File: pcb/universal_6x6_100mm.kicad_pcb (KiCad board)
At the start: 2 copper layers, 100 x 100 mm, 88 parts

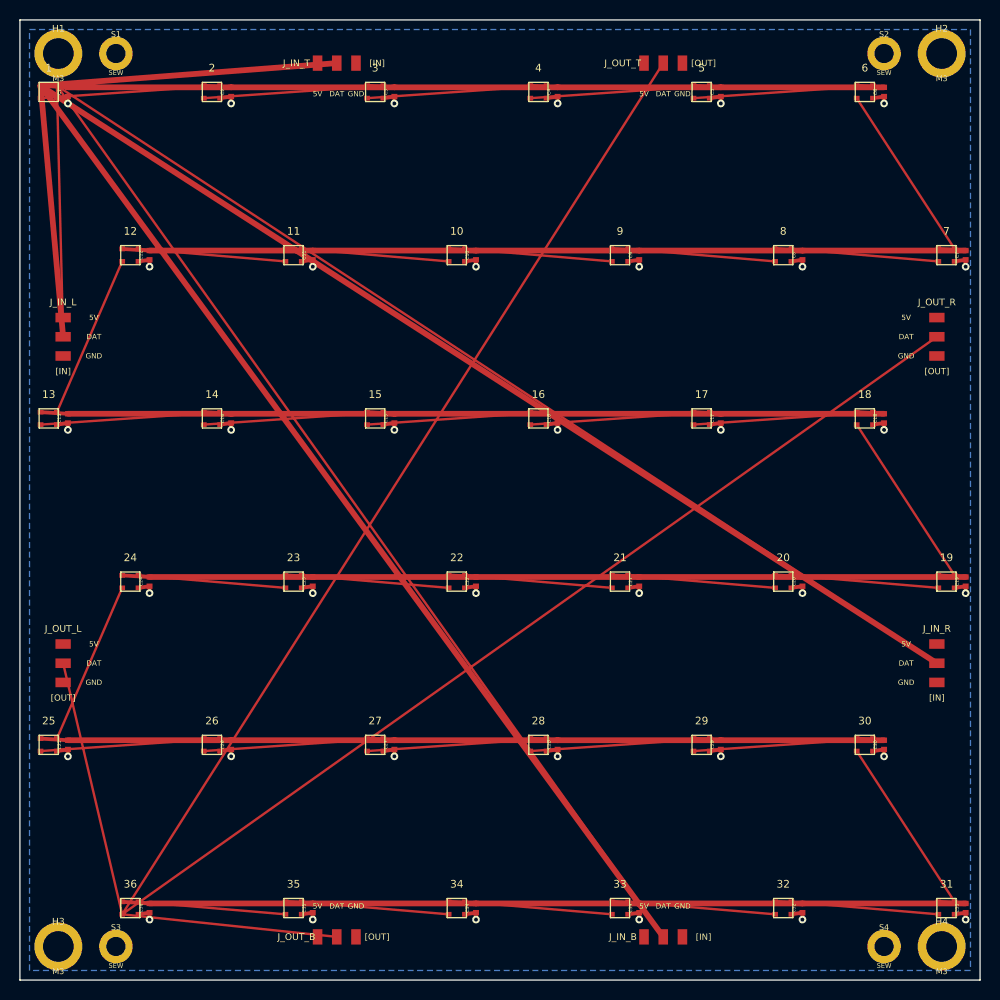
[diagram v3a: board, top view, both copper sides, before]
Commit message: feat: set back 8-port JST matrix 10mm into valleys for diagonal 50mm cable fit and zero overlap
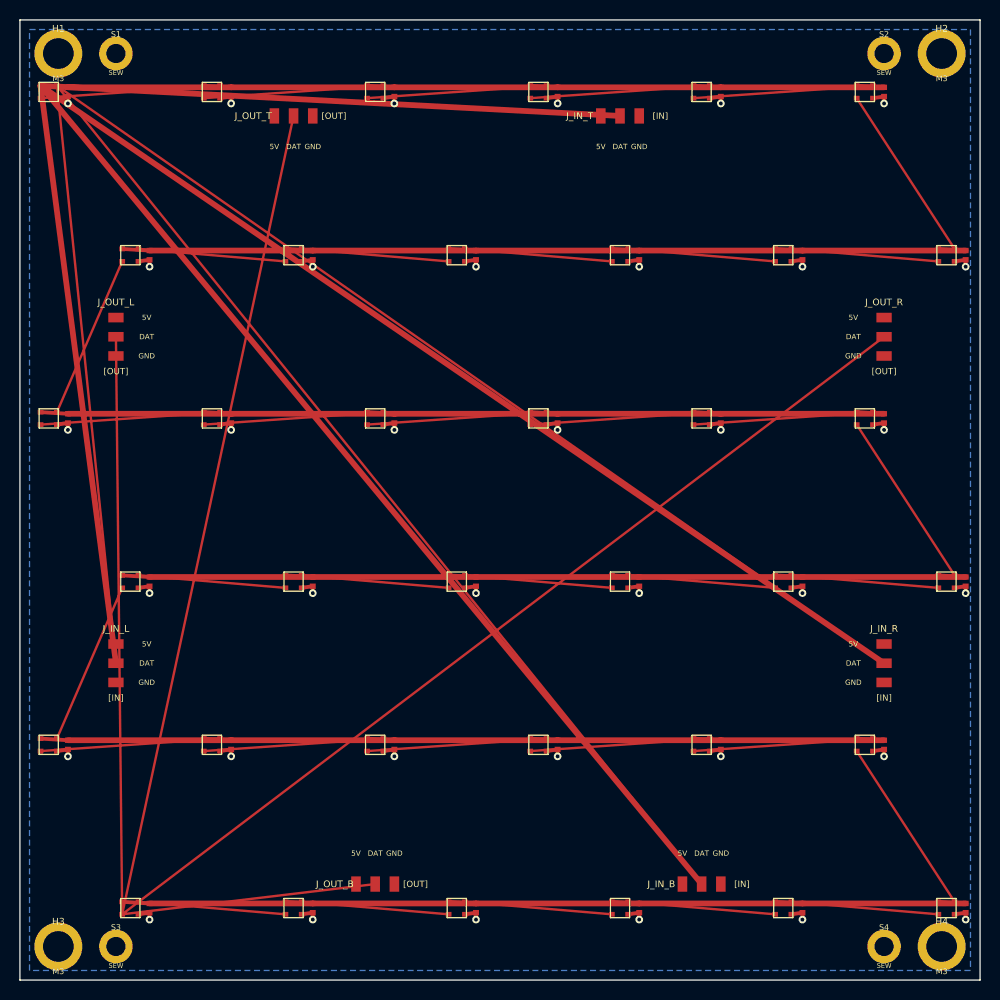
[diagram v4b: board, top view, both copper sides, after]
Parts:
- removed 1, 10, 11, 12, 13, 14, 15, 16, 17, 18, 19, 2, 20, 21, 22, 23, 24, 25, 26, 27, 28, 29, 3, 30, 31, 32, 33, 34, 35, 36, 4, 5, 6, 7, 8, 9: , LED_SMD:LED_WS2812B_PLCC4_2.0x2.0mm
- added D1: , LED_SMD:LED_WS2812B_PLCC4_2.0x2.0mm, F.Cu at (3.00, 7.50)
- added D10: , LED_SMD:LED_WS2812B_PLCC4_2.0x2.0mm, F.Cu at (45.5, 24.5)
- added D11: , LED_SMD:LED_WS2812B_PLCC4_2.0x2.0mm, F.Cu at (28.5, 24.5)
- added D12: , LED_SMD:LED_WS2812B_PLCC4_2.0x2.0mm, F.Cu at (11.5, 24.5)
- added D13: , LED_SMD:LED_WS2812B_PLCC4_2.0x2.0mm, F.Cu at (3.00, 41.5)
- added D14: , LED_SMD:LED_WS2812B_PLCC4_2.0x2.0mm, F.Cu at (20.0, 41.5)
- added D15: , LED_SMD:LED_WS2812B_PLCC4_2.0x2.0mm, F.Cu at (37.0, 41.5)
- added D16: , LED_SMD:LED_WS2812B_PLCC4_2.0x2.0mm, F.Cu at (54.0, 41.5)
- added D17: , LED_SMD:LED_WS2812B_PLCC4_2.0x2.0mm, F.Cu at (71.0, 41.5)
- added D18: , LED_SMD:LED_WS2812B_PLCC4_2.0x2.0mm, F.Cu at (88.0, 41.5)
- added D19: , LED_SMD:LED_WS2812B_PLCC4_2.0x2.0mm, F.Cu at (96.5, 58.5)
- added D2: , LED_SMD:LED_WS2812B_PLCC4_2.0x2.0mm, F.Cu at (20.0, 7.50)
- added D20: , LED_SMD:LED_WS2812B_PLCC4_2.0x2.0mm, F.Cu at (79.5, 58.5)
- added D21: , LED_SMD:LED_WS2812B_PLCC4_2.0x2.0mm, F.Cu at (62.5, 58.5)
- added D22: , LED_SMD:LED_WS2812B_PLCC4_2.0x2.0mm, F.Cu at (45.5, 58.5)
- added D23: , LED_SMD:LED_WS2812B_PLCC4_2.0x2.0mm, F.Cu at (28.5, 58.5)
- added D24: , LED_SMD:LED_WS2812B_PLCC4_2.0x2.0mm, F.Cu at (11.5, 58.5)
- added D25: , LED_SMD:LED_WS2812B_PLCC4_2.0x2.0mm, F.Cu at (3.00, 75.5)
- added D26: , LED_SMD:LED_WS2812B_PLCC4_2.0x2.0mm, F.Cu at (20.0, 75.5)
- added D27: , LED_SMD:LED_WS2812B_PLCC4_2.0x2.0mm, F.Cu at (37.0, 75.5)
- added D28: , LED_SMD:LED_WS2812B_PLCC4_2.0x2.0mm, F.Cu at (54.0, 75.5)
- added D29: , LED_SMD:LED_WS2812B_PLCC4_2.0x2.0mm, F.Cu at (71.0, 75.5)
- added D3: , LED_SMD:LED_WS2812B_PLCC4_2.0x2.0mm, F.Cu at (37.0, 7.50)
- added D30: , LED_SMD:LED_WS2812B_PLCC4_2.0x2.0mm, F.Cu at (88.0, 75.5)
- added D31: , LED_SMD:LED_WS2812B_PLCC4_2.0x2.0mm, F.Cu at (96.5, 92.5)
- added D32: , LED_SMD:LED_WS2812B_PLCC4_2.0x2.0mm, F.Cu at (79.5, 92.5)
- added D33: , LED_SMD:LED_WS2812B_PLCC4_2.0x2.0mm, F.Cu at (62.5, 92.5)
- added D34: , LED_SMD:LED_WS2812B_PLCC4_2.0x2.0mm, F.Cu at (45.5, 92.5)
- added D35: , LED_SMD:LED_WS2812B_PLCC4_2.0x2.0mm, F.Cu at (28.5, 92.5)
- added D36: , LED_SMD:LED_WS2812B_PLCC4_2.0x2.0mm, F.Cu at (11.5, 92.5)
- added D4: , LED_SMD:LED_WS2812B_PLCC4_2.0x2.0mm, F.Cu at (54.0, 7.50)
- added D5: , LED_SMD:LED_WS2812B_PLCC4_2.0x2.0mm, F.Cu at (71.0, 7.50)
- added D6: , LED_SMD:LED_WS2812B_PLCC4_2.0x2.0mm, F.Cu at (88.0, 7.50)
- added D7: , LED_SMD:LED_WS2812B_PLCC4_2.0x2.0mm, F.Cu at (96.5, 24.5)
- added D8: , LED_SMD:LED_WS2812B_PLCC4_2.0x2.0mm, F.Cu at (79.5, 24.5)
- added D9: , LED_SMD:LED_WS2812B_PLCC4_2.0x2.0mm, F.Cu at (62.5, 24.5)
- moved J_OUT_T 38.9 mm to (28.5, 10.0)
- moved J_IN_L 34.4 mm to (10.0, 67.0)
- moved J_OUT_L 34.4 mm to (10.0, 33.0)
- moved J_IN_T 30.0 mm to (62.5, 10.0)
- moved J_IN_B 6.80 mm to (71.0, 90.0)
- moved J_OUT_B 6.80 mm to (37.0, 90.0)
- moved J_IN_R 5.50 mm to (90.0, 67.0)
- moved J_OUT_R 5.50 mm to (90.0, 33.0)
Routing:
- net +5V: track 890.9 -> 948.3 mm
- net DATA_1: track 273.9 -> 331.1 mm
- net DATA_37: track 258.4 -> 271.3 mm
